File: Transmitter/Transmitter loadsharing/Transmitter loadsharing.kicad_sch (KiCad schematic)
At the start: 20 parts, among them J1 Conn_Coaxial, J2 Conn_01x02, J3 Conn_01x03, J4 Conn_01x02_Socket, J5 Conn_01x02, J6 Conn_01x01, U1 OPA3692IDBQR

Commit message: mostly changes to transmitter prototype, for using the prototyper
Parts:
- removed C8, C9: 6.8 uF, Capacitor_SMD:C_0805_2012Metric_Pad1.18x1.45mm_HandSolder, symbol Device:C
- removed J2: Conn_01x02, Connector_PinHeader_2.54mm:PinHeader_1x02_P2.54mm_Vertical, symbol Connector_Generic:Conn_01x02
- added C10, C14, C18, C22: 6.8 uF, Capacitor_SMD:C_0805_2012Metric_Pad1.18x1.45mm_HandSolder, symbol Device:C
- added C11, C12, C13, C15, C16, C17, C19, C20, C21, C23, C24, C25: 0.1 nF, Capacitor_SMD:C_0805_2012Metric_Pad1.18x1.45mm_HandSolder, symbol Device:C
- added J7: Conn_01x02, Connector_PinHeader_2.54mm:PinHeader_1x02_P2.54mm_Vertical, symbol Connector_Generic:Conn_01x02
- added J8: Conn_01x02_Socket, Connector_PinSocket_2.54mm:PinSocket_1x02_P2.54mm_Vertical, symbol Connector:Conn_01x02_Socket
- added R10, R18, R19, R20, R4, R7: R, Resistor_SMD:R_0805_2012Metric_Pad1.20x1.40mm_HandSolder, symbol Device:R
- added R11, R21: 1 Ohm, Resistor_SMD:R_0805_2012Metric_Pad1.20x1.40mm_HandSolder, symbol Device:R
- added R12, R13, R14, R3, R5, R8: 250 Ohm, Resistor_SMD:R_0805_2012Metric_Pad1.20x1.40mm_HandSolder, symbol Device:R
- added R15, R16, R17, R2, R6, R9: 1 kOhm, Resistor_SMD:R_0805_2012Metric_Pad1.20x1.40mm_HandSolder, symbol Device:R
- added U2, U3, U4, U5, U6, U7: THS3091D, THS3091DDR:DDA8_2P28X2P28, symbol THS3091:THS3091D
- U1: footprint DBQ16 -> Opa3962:DBQ16
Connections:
- net +5V: now also C10.1, C13.2, C15.2, C17.2, C18.1, C23.2, C24.2, C25.2, U2.7 (VS+), U3.7 (VS+), U4.7 (VS+), U5.7 (VS+), U6.7 (VS+), U7.7 (VS+)
- net -5V: now also J3.1 (Pin_1), C11.1, C12.1, C14.1, C16.1, C19.1, C20.1, C21.1, C22.1, U2.4 (VS-), U3.4 (VS-), U4.4 (VS-), U5.4 (VS-), U6.4 (VS-), U7.4 (VS-); no longer J3.2 (Pin_2)
- net GND: now also J3.2 (Pin_2), C10.2, C11.2, C12.2, C13.1, C14.2, C15.1, C16.2, C17.1, C18.2, C19.2, C20.2, C21.2, C22.2, C23.1, C24.1, C25.1, R12.1, R13.1, R14.1, R3.1, R5.1, R8.1; no longer J3.1 (Pin_1)
- net coil end: now also R21.1
- net coil start: now also R11.1
- new net: R2.1, R4.1, U2.6 (VOUT)
- new net: R2.2, R3.2, U2.2 (VIN-)
- new net: R15.1, R18.1, U5.6 (VOUT)
- new net: R12.2, R15.2, U5.2 (VIN-)
- new net: R6.1, R7.1, U3.6 (VOUT)
- new net: R5.2, R6.2, U3.2 (VIN-)
- new net: R14.2, R17.2, U7.2 (VIN-)
- new net: R17.1, R20.1, U7.6 (VOUT)
- new net: R8.2, R9.2, U4.2 (VIN-)
- new net: R10.1, R9.1, U4.6 (VOUT)
- new net: R16.1, R19.1, U6.6 (VOUT)
- new net: R13.2, R16.2, U6.2 (VIN-)
- new net coil load end: J7.2 (Pin_2), J8.2 (Pin_2), R18.2, R19.2, R20.2
- new net coil load start: J7.1 (Pin_1), J8.1 (Pin_1), R10.2, R4.2, R7.2
- new net loadshare input +: R11.2, U2.3 (VIN+), U3.3 (VIN+), U4.3 (VIN+)
- new net loadshare input -: R21.2, U5.3 (VIN+), U6.3 (VIN+), U7.3 (VIN+)
- no-connect marks 5 -> 23
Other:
- removed sheet loadsharing

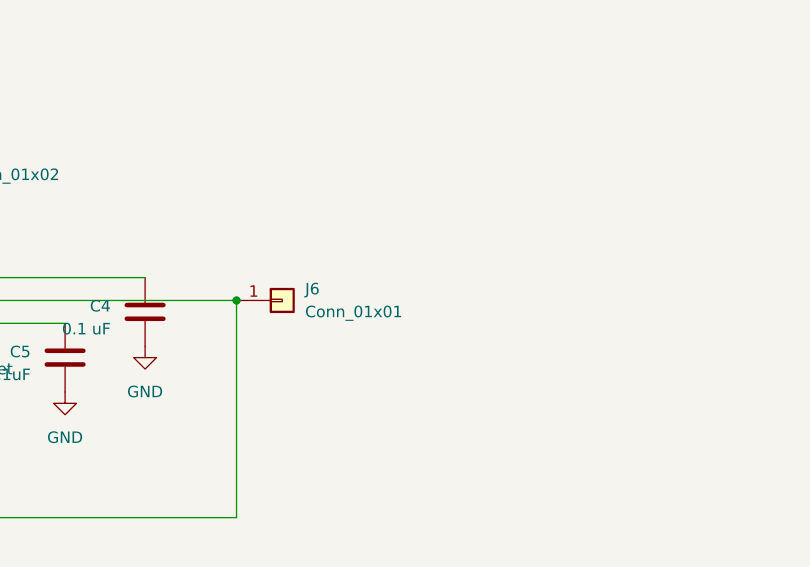
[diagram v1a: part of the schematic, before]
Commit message: added footprints for SOIC and SSOP for OPA3692
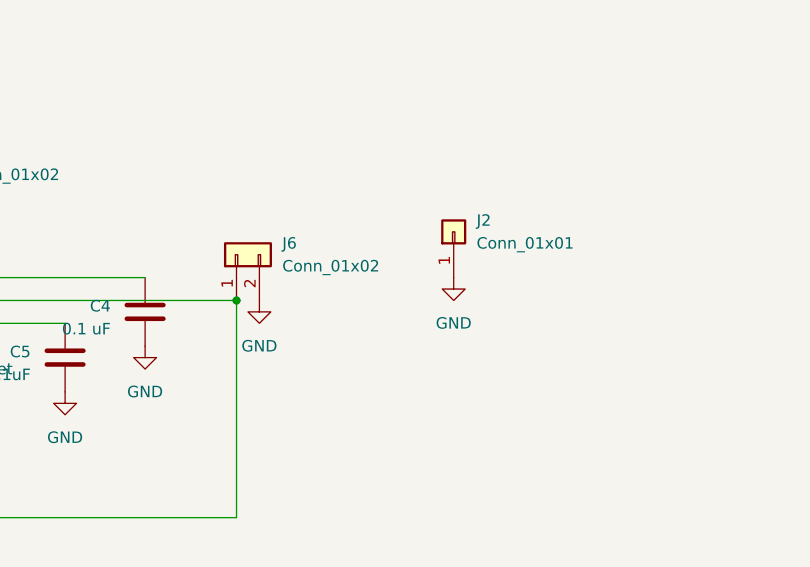
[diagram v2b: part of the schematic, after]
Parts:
- removed J6: Conn_01x01, Connector_PinHeader_2.54mm:PinHeader_1x01_P2.54mm_Vertical, symbol Connector_Generic:Conn_01x01
- added J2: Conn_01x01, Connector_PinHeader_2.54mm:PinHeader_1x01_P2.54mm_Vertical, symbol Connector_Generic:Conn_01x01
- added J6: Conn_01x02, Connector_PinHeader_2.54mm:PinHeader_1x02_P2.54mm_Vertical, symbol Connector_Generic:Conn_01x02
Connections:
- net GND: now also J2.1 (Pin_1), J6.2 (Pin_2)
- net at U1.14 (OUTA), U1.5 (INB+), U1.7 (INC-): now also J6.1 (Pin_1)
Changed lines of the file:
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@@
 	)
 	(junction
-		(at 217.17 97.79)
-		(diameter 0)
-		(color 0 0 0 0)
-	)
-	(junction
 		(at 119.38 57.15)
 		(diameter 0)
@@
 	)
 	(junction
+		(at 217.17 97.79)
+		(diameter 0)
+		(color 0 0 0 0)
+	)
+	(junction
 		(at 118.11 67.31)
 		(diameter 0)
@@
 	)
 	(symbol
-		(lib_id "Device:C")
-		(at 182.88 252.73 0)
+		(lib_id "Connector_Generic:Conn_01x01")
+		(at 241.3 90.17 90)
 		(unit 1)
 		(exclude_from_sim no)
@@
 		(dnp no)
 		(fields_autoplaced yes)
-		(property "Reference" "C19"
-			(at 186.69 251.4599 0)
+		(property "Reference" "J2"
+			(at 243.84 88.8999 90)
 			(effects
 				(font
 					(size 1.27 1.27)
 				)
-				(justify left)
+				(justify right)
 			)
 		)
-		(property "Value" "0.1 nF"
-			(at 186.69 253.9999 0)
+		(property "Value" "Conn_01x01"
+			(at 243.84 91.4399 90)
 			(effects
 				(font
 					(size 1.27 1.27)
 				)
-				(justify left)
+				(justify right)
 			)
 		)
-		(property "Footprint" "Capacitor_SMD:C_0805_2012Metric_Pad1.18x1.45mm_HandSolder"
-			(at 183.8452 256.54 0)
+		(property "Footprint" "Connector_PinHeader_2.54mm:PinHeader_1x01_P2.54mm_Vertical"
+			(at 241.3 90.17 0)
 			(effects
 				(font
@@
 		)
 		(property "Datasheet" "~"
-			(at 182.88 252.73 0)
+			(at 241.3 90.17 0)
 			(effects
 				(font
@@
 			)
 		)
-		(property "Description" "Unpolarized capacitor"
-			(at 182.88 252.73 0)
+		(property "Description" "Generic connector, single row, 01x01, script generated (kicad-library-utils/schlib/autogen/connector/)"
+			(at 241.3 90.17 0)
 			(effects
 				(font
@@
 			)
 		)
-		(pin "2"
-		)
 		(pin "1"
 		)
@@
 			(project "Transmitter loadsharing"
 				(path "/4dee756a-58e7-4e26-8fbe-661c6c218f1e"
-					(reference "C19")
+					(reference "J2")
 					(unit 1)
 				)
@@
 	)
 	(symbol
-		(lib_id "Connector_Generic:Conn_01x01")
-		(at 222.25 97.79 0)
+		(lib_id "Device:C")
+		(at 182.88 252.73 0)
 		(unit 1)
 		(exclude_from_sim no)
@@
 		(dnp no)
 		(fields_autoplaced yes)
-		(property "Reference" "J6"
-			(at 224.79 96.5199 0)
+		(property "Reference" "C19"
+			(at 186.69 251.4599 0)
 			(effects
 				(font
@@
 			)
 		)
-		(property "Value" "Conn_01x01"
-			(at 224.79 99.0599 0)
+		(property "Value" "0.1 nF"
+			(at 186.69 253.9999 0)
 			(effects
 				(font
@@
 			)
 		)
-		(property "Footprint" "Connector_PinHeader_2.54mm:PinHeader_1x01_P2.54mm_Vertical"
-			(at 222.25 97.79 0)
+		(property "Footprint" "Capacitor_SMD:C_0805_2012Metric_Pad1.18x1.45mm_HandSolder"
+			(at 183.8452 256.54 0)
 			(effects
 				(font
@@
 		)
 		(property "Datasheet" "~"
-			(at 222.25 97.79 0)
+			(at 182.88 252.73 0)
 			(effects
 				(font
@@
 			)
 		)
-		(property "Description" "Generic connector, single row, 01x01, script generated (kicad-library-utils/schlib/autogen/connector/)"
-			(at 222.25 97.79 0)
+		(property "Description" "Unpolarized capacitor"
+			(at 182.88 252.73 0)
 			(effects
 				(font
@@
 			)
 		)
+		(pin "2"
+		)
 		(pin "1"
 		)
@@
 			(project "Transmitter loadsharing"
 				(path "/4dee756a-58e7-4e26-8fbe-661c6c218f1e"
-					(reference "J6")
-					(unit 1)
-				)
-			)
-			(project "Transmitter prototype"
-				(path "/c11cda7e-a7f0-42b6-b4a5-7aa6ec037d29"
-					(reference "J6")
+					(reference "C19")
 					(unit 1)
 				)
@@
 	)
 	(symbol
+		(lib_id "Connector_Generic:Conn_01x02")
+		(at 217.17 92.71 90)
+		(unit 1)
+		(exclude_from_sim no)
+		(in_bom yes)
+		(on_board yes)
+		(dnp no)
+		(fields_autoplaced yes)
+		(property "Reference" "J6"
+			(at 222.25 91.4399 90)
+			(effects
+				(font
+					(size 1.27 1.27)
+				)
+				(justify right)
+			)
+		)
+		(property "Value" "Conn_01x02"
+			(at 222.25 93.9799 90)
+			(effects
+				(font
+					(size 1.27 1.27)
+				)
+				(justify right)
+			)
+		)
+		(property "Footprint" "Connector_PinHeader_2.54mm:PinHeader_1x02_P2.54mm_Vertical"
+			(at 217.17 92.71 0)
+			(effects
+				(font
+					(size 1.27 1.27)
+				)
+				(hide yes)
+			)
+		)
+		(property "Datasheet" "~"
+			(at 217.17 92.71 0)
+			(effects
+				(font
+					(size 1.27 1.27)
+				)
+				(hide yes)
+			)
+		)
+		(property "Description" "Generic connector, single row, 01x02, script generated (kicad-library-utils/schlib/autogen/connector/)"
+			(at 217.17 92.71 0)
+			(effects
+				(font
+					(size 1.27 1.27)
+				)
+				(hide yes)
+			)
+		)
+		(pin "2"
+		)
+		(pin "1"
+		)
+		(instances
+			(project "Transmitter loadsharing"
+				(path "/4dee756a-58e7-4e26-8fbe-661c6c218f1e"
+					(reference "J6")
+					(unit 1)
+				)
+			)
+		)
+	)
+	(symbol
 		(lib_id "Device:C")
 		(at 31.75 251.46 0)
@@
 	)
 	(symbol
+		(lib_name "GND_1")
+		(lib_id "power:GND")
+		(at 219.71 97.79 0)
+		(unit 1)
+		(exclude_from_sim no)
+		(in_bom yes)
+		(on_board yes)
+		(dnp no)
+		(fields_autoplaced yes)
+		(property "Reference" "#PWR023"
+			(at 219.71 104.14 0)
+			(effects
+				(font
+					(size 1.27 1.27)
+				)
+				(hide yes)
+			)
+		)
+		(property "Value" "GND"
+			(at 219.71 102.87 0)
+			(effects
+				(font
+					(size 1.27 1.27)
+				)
+			)
+		)
+		(property "Footprint" ""
+			(at 219.71 97.79 0)
+			(effects
+				(font
+					(size 1.27 1.27)
+				)
+				(hide yes)
+			)
+		)
+		(property "Datasheet" ""
+			(at 219.71 97.79 0)
+			(effects
+				(font
+					(size 1.27 1.27)
+				)
+				(hide yes)
+			)
+		)
+		(property "Description" "Power symbol creates a global label with name \"GND\" , ground"
+			(at 219.71 97.79 0)
+			(effects
+				(font
+					(size 1.27 1.27)
+				)
+				(hide yes)
+			)
+		)
+		(pin "1"
+		)
+		(instances
+			(project "Transmitter loadsharing"
+				(path "/4dee756a-58e7-4e26-8fbe-661c6c218f1e"
+					(reference "#PWR023")
+					(unit 1)
+				)
+			)
+		)
+	)
+	(symbol
 		(lib_id "Device:C")
 		(at 30.48 151.13 0)
@@
 					(unit 1)
 				)
+			)
+		)
+	)
+	(symbol
+		(lib_name "GND_1")
+		(lib_id "power:GND")
+		(at 241.3 95.25 0)
+		(unit 1)
+		(exclude_from_sim no)
+		(in_bom yes)
+		(on_board yes)
+		(dnp no)
+		(fields_autoplaced yes)
+		(property "Reference" "#PWR034"
+			(at 241.3 101.6 0)
+			(effects
+				(font
+					(size 1.27 1.27)
+				)
+				(hide yes)
+			)
+		)
+		(property "Value" "GND"
+			(at 241.3 100.33 0)
+			(effects
+				(font
+					(size 1.27 1.27)
+				)
+			)
+		)
+		(property "Footprint" ""
+			(at 241.3 95.25 0)
+			(effects
+				(font
+					(size 1.27 1.27)
+				)
+				(hide yes)
+			)
+		)
+		(property "Datasheet" ""
+			(at 241.3 95.25 0)
+			(effects
+				(font
+					(size 1.27 1.27)
+				)
+				(hide yes)
+			)
+		)
+		(property "Description" "Power symbol creates a global label with name \"GND\" , ground"
+			(at 241.3 95.25 0)
+			(effects
+				(font
+					(size 1.27 1.27)
+				)
+				(hide yes)
+			)
+		)
+		(pin "1"
+		)
+		(instances
+			(project "Transmitter loadsharing"
+				(path "/4dee756a-58e7-4e26-8fbe-661c6c218f1e"
+					(reference "#PWR034")
+					(unit 1)
+				)

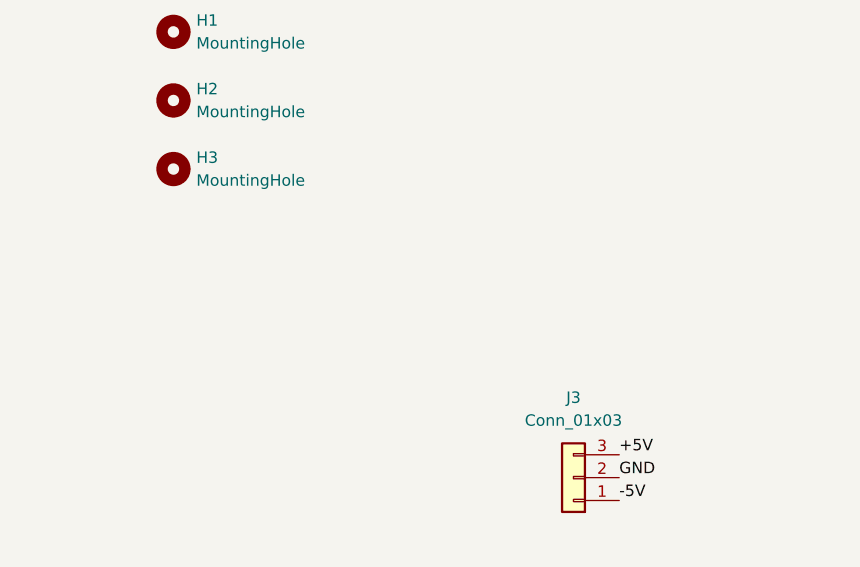
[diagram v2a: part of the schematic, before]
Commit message: added 3d models for OPA3692, THS3091 and BNC connector
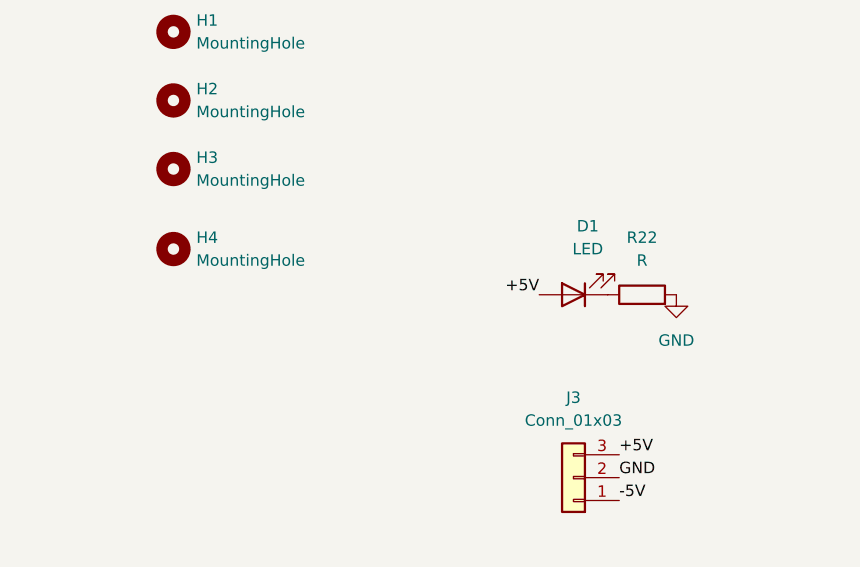
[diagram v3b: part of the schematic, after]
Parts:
- added D1: LED, LED_SMD:LED_0805_2012Metric_Pad1.15x1.40mm_HandSolder, symbol Device:LED
- added H4: MountingHole, MountingHole:MountingHole_3.2mm_M3_Pad, symbol Mechanical:MountingHole
- added R22: R, Resistor_SMD:R_0805_2012Metric_Pad1.20x1.40mm_HandSolder, symbol Device:R
- H1, H2, H3: footprint MountingHole:MountingHole_2.5mm_Pad -> MountingHole:MountingHole_3.2mm_M3_Pad
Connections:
- net +5V: now also D1.2 (A)
- net GND: now also R22.2
- new net: D1.1 (K), R22.1

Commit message: First revision of Tx board
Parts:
- removed J2: Conn_01x01, Connector_PinHeader_2.54mm:PinHeader_1x01_P2.54mm_Vertical, symbol Connector_Generic:Conn_01x01
- removed J6: Conn_01x02, Connector_PinHeader_2.54mm:PinHeader_1x02_P2.54mm_Vertical, symbol Connector_Generic:Conn_01x02
- added C26, C30: 0.47u, Capacitor_SMD:C_0603_1608Metric_Pad1.08x0.95mm_HandSolder, symbol Device:C
- added C27, C28, C31, C32, C9: 10u, Capacitor_SMD:C_0603_1608Metric_Pad1.08x0.95mm_HandSolder, symbol Device:C
- added C29: 22u, Capacitor_SMD:C_0603_1608Metric_Pad1.08x0.95mm_HandSolder, symbol Device:C
- added D2: LED, LED_SMD:LED_0603_1608Metric_Pad1.05x0.95mm_HandSolder, symbol Device:LED
- added J10, J11, J12, J13, J14, J15, J16, J20, J21, J22, J23, J6, J9: Conn_01x01, Connector_PinHeader_2.54mm:PinHeader_1x01_P2.54mm_Vertical, symbol Connector_Generic:Conn_01x01
- added J17, J18: Conn_Coaxial, Connector_Coaxial:BNC_Amphenol_B6252HB-NPP3G-50_Horizontal, symbol Connector:Conn_Coaxial
- added J19: Conn_Coaxial, 132289 SMA:CONN_132289_AMP, symbol Connector:Conn_Coaxial
- added J2: Conn_01x03, Connector_PinHeader_2.54mm:PinHeader_1x03_P2.54mm_Vertical, symbol Connector_Generic:Conn_01x03
- added R23, R29, R31, R33, R35, R37, R39: R, Resistor_SMD:R_0603_1608Metric_Pad0.98x0.95mm_HandSolder, symbol Device:R
- added R24, R25, R26: 50 Ohm, Resistor_SMD:R_0603_1608Metric_Pad0.98x0.95mm_HandSolder, symbol Device:R
- added R28, R30, R32, R34, R36, R38: 0 Ohm, Resistor_SMD:R_0603_1608Metric_Pad0.98x0.95mm_HandSolder, symbol Device:R
- added R40, R41: 24.9k, Resistor_SMD:R_0603_1608Metric_Pad0.98x0.95mm_HandSolder, symbol Device:R
- added U10, U11: LT3094EMSE-PBF, LT3094:05-08-1666_ADI, symbol LT3094:LT3094EMSE-PBF
- added U8, U9: LT3045EMSE-PBF, LT3045:MSOP12_MSE_ADI, symbol LT3045 MSOP:LT3045EMSE-PBF
- C1, C10, C11, C12, C13, C14, C15, C16, C17, C18, C19, C2, C20, C21, C22, C23, C24, C25, C3, C4, C5, C6, C7: footprint Capacitor_SMD:C_0805_2012Metric_Pad1.18x1.45mm_HandSolder -> Capacitor_SMD:C_0603_1608Metric_Pad1.08x0.95mm_HandSolder
- D1: footprint LED_SMD:LED_0805_2012Metric_Pad1.15x1.40mm_HandSolder -> LED_SMD:LED_0603_1608Metric_Pad1.05x0.95mm_HandSolder
- J1: footprint Amphenol 112404:CONN_112404_AMP -> 132289 SMA:CONN_132289_AMP
- R10, R11, R12, R13, R14, R15, R16, R17, R18, R19, R2, R20, R21, R22, R3, R4, R5, R6, R7, R8, R9: footprint Resistor_SMD:R_0805_2012Metric_Pad1.20x1.40mm_HandSolder -> Resistor_SMD:R_0603_1608Metric_Pad0.98x0.95mm_HandSolder
- U1: footprint Opa3962:DBQ16 -> Opa3692 SOIC:DBQ16
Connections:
- net +5V: now also J2.2 (Pin_2); no longer J3.3 (Pin_3)
- net -5V: now also J3.2 (Pin_2), D2.2 (A); no longer J3.1 (Pin_1)
- net GND: now also C26.2, C27.2, C28.2, C29.2, C30.2, C31.2, C32.2, C9.2, J10.1 (Pin_1), J11.1 (Pin_1), J12.1 (Pin_1), J13.1 (Pin_1), J14.1 (Pin_1), J15.1 (Pin_1), J16.1 (Pin_1), J17.2 (Ext), J18.2 (Ext), J19.2 (Ext), J9.1 (Pin_1), R23.2, R29.1, R31.1, R33.1, R35.1, R37.1, R39.1, R40.2, R41.2, U10.13 (IN), U10.6 (ILIM), U10.9 (GND), U11.13 (IN), U11.6 (ILIM), U11.9 (GND), U8.6 (ILIM), U8.9 (GND), U8.EPAD (GND), U9.6 (ILIM), U9.9 (GND), U9.EPAD (GND); no longer J3.2 (Pin_2)
- net loadshare input +: now also R28.1, R30.1, R32.1; no longer U2.3 (VIN+), U3.3 (VIN+), U4.3 (VIN+)
- net loadshare input -: now also R34.1, R36.1, R38.1; no longer U5.3 (VIN+), U6.3 (VIN+), U7.3 (VIN+)
- net at U1.14 (OUTA), U1.5 (INB+), U1.7 (INC-): now also J6.1 (Pin_1)
- net at C1.1: now also J23.1 (Pin_1), R25.2, R26.2; no longer J1.1 (In)
- new net: D2.1 (K), R23.1
- new net: R30.2, R31.2, U3.3 (VIN+)
- new net: C26.1, R40.1, U8.8 (SET), U9.8 (SET)
- new net: R34.2, R35.2, U6.3 (VIN+)
- new net: R36.2, R37.2, U7.3 (VIN+)
- new net: C30.1, R41.1, U10.8 (SET), U11.8 (SET)
- new net: R38.2, R39.2, U5.3 (VIN+)
- new net: R32.2, R33.2, U4.3 (VIN+)
- new net: R28.2, R29.2, U2.3 (VIN+)
- new net +5V_In: C27.1, C28.1, J2.1 (Pin_1), U8.10 (OUTS), U8.11 (OUT), U9.10 (OUTS), U9.11 (OUT)
- new net -5V_In: C31.1, C32.1, J3.1 (Pin_1), U10.10 (OUTS), U10.11 (OUT), U11.10 (OUTS), U11.11 (OUT)
- new net PWR+: C9.1, J17.1 (In), J2.3 (Pin_3), J20.1 (Pin_1), U8.1 (IN), U8.4 (EN/UV), U8.7 (PGFB), U9.1 (IN), U9.4 (EN/UV), U9.7 (PGFB)
- new net PWR-: C29.1, J18.1 (In), J21.1 (Pin_1), J3.3 (Pin_3), U10.1 (IN), U10.3 (EN/UV), U10.5 (PGFB), U11.1 (IN), U11.3 (EN/UV), U11.5 (PGFB)
- new net Ref out: J19.1 (In), J22.1 (Pin_1), R24.2, R25.1
- new net Signal in: J1.1 (In), R24.1, R26.1
- no-connect marks 23 -> 39
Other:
- note added: "+5V regulator circut"
- note added: "-5V regulator circut"
- note added: "Loadsharing circuit"
- note added: "Radio splitter and phase shift circuit"
- moved on the sheet: C1, C10, C11, C12, C13, C14, C15, C16, C17, C18, C19, C20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

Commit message: Small corrections, changed footprint for edge SMA connectors
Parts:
- J1, J19: footprint 132289 SMA:CONN_132289_AMP -> Connector_Coaxial:SMA_Amphenol_132289_EdgeMount
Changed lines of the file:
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@@
 			)
 		)
-		(property "Footprint" "132289 SMA:CONN_132289_AMP"
+		(property "Footprint" "Connector_Coaxial:SMA_Amphenol_132289_EdgeMount"
 			(at 22.86 83.82 0)
 			(effects
@@
 			)
 		)
-		(property "Footprint" "132289 SMA:CONN_132289_AMP"
+		(property "Footprint" "Connector_Coaxial:SMA_Amphenol_132289_EdgeMount"
 			(at 21.59 107.95 0)
 			(effects
